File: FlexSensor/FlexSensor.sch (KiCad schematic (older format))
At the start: 167 parts

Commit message: Added ethernet
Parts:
- added C?: 470pF, symbol Device:C_Small
- added C?: 1µF, symbol Device:C_Small
- added C?: 4.7µF, symbol Device:C_Small
- added C? (x4): 100nF, symbol Device:C_Small
- added C?: 22nF, symbol Device:C_Small
- added J?: 8P8C_LED, symbol Connector:8P8C_LED
- added L?: FB 2.0A/0.050 DCR, symbol Device:Ferrite_Bead_Small
- added R? (x2): 330, symbol Device:R
- added R?: 100, symbol Device:R
- added R?: 12K, symbol Device:R
- added R? (x4): 49.9, symbol Device:R
- added R? (x2): 33, symbol Device:R
- added U?: LAN8720A, Package_DFN_QFN:QFN-24-1EP_4x4mm_P0.5mm_EP2.6x2.6mm, symbol Interface_Ethernet:LAN8720A
- added U?: JYSP75S4, symbol Trainiot:JYSP75S4
- R? (x2): value 10K -> 12K
- R?: value 10K -> 36K
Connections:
- net labels added: BOOTED, ETH_LED1, ETH_LED2
- net labels removed: RMII_EXT_OSC_CLK
- wire segments 864 -> 961
- no-connect marks 24 -> 28
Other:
- note added: "Check which led is 1 and which is 2 in the pinout"
- note added: "Ethernet"
- note added: "Just an inverter, can\nbe replaced"
- moved on the sheet: C?, D?, Q?, R?, U?, U?A

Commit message: Added pull up to shift register output for S88
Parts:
- added R? (x4): 36K, symbol Device:R
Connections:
- wire segments 961 -> 973
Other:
- moved on the sheet: C?, U?

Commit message: Working on adding LocoNet
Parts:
- removed U?: ULN2003A, symbol Transistor_Array:ULN2003A
- added C?: 4.7µF, symbol Device:C_Small
- added D?: 1N4148, Diode_THT:D_DO-35_SOD27_P7.62mm_Horizontal, symbol Diode:1N4148
- added D? (x2): LED, symbol Device:LED
- added J? (x2): 6P6C, symbol Connector:6P6C
- added Q?: BC817, Package_TO_SOT_SMD:SOT-23, symbol Transistor_BJT:BC817
- added R?: 27K, symbol Device:R
- added R?: 180K, symbol Device:R
- added R? (x2): 10K, symbol Device:R
- added R?: 240K, symbol Device:R
- added R?: 56K, symbol Device:R
- added R?: 22K, symbol Device:R
- added R?: 1K, symbol Device:R
- added R? (x2): 330, symbol Device:R
- added U?: ULN2803A, symbol Transistor_Array:ULN2803A
- added U? (x2): LM393, symbol Comparator:LM393
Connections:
- net labels added: PULL_DOWN_0, PULL_DOWN_1
- net labels removed: PULL_DOWN
- wire segments 973 -> 1056
- no-connect marks 28 -> 27
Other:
- note added: "Invert????????????????"
- note added: "Transmit LED? Maybe use fact tx and rx are identical in transmit?"
- note removed: "Cheap level shifter without pullup?"
- note removed: "ULN2803A could drive a second pull down,\nfor 3 different pull down values \nusing one extra GPIO pin."
- moved on the sheet: R?

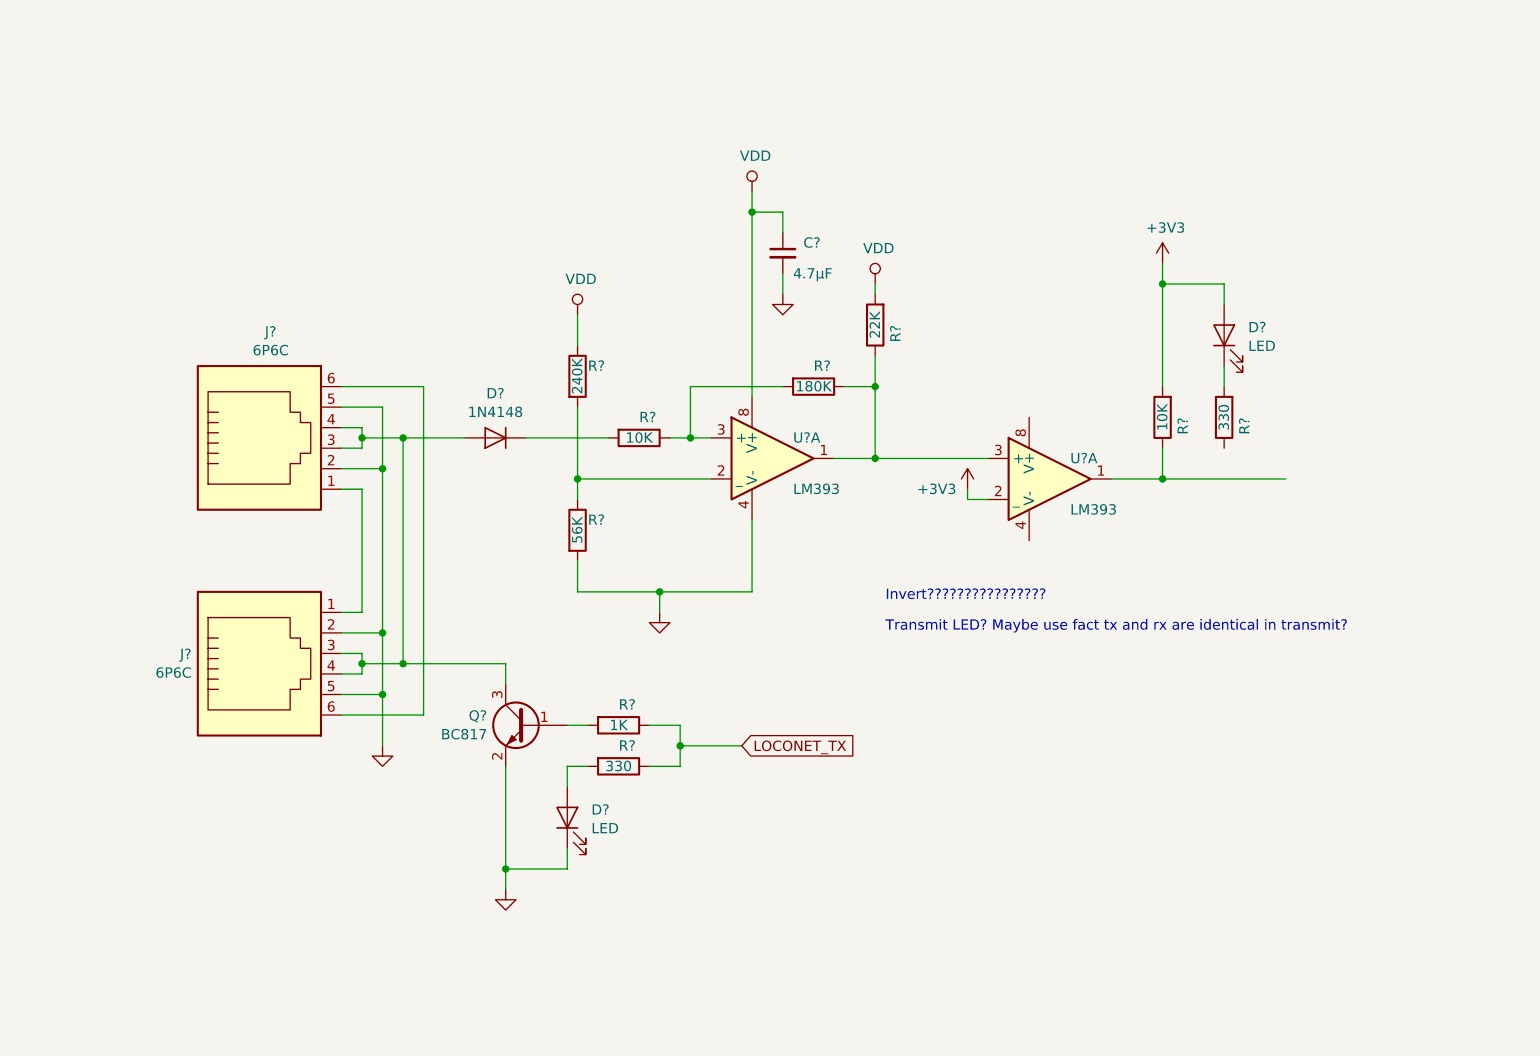
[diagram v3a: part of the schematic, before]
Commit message: Added LocoNet
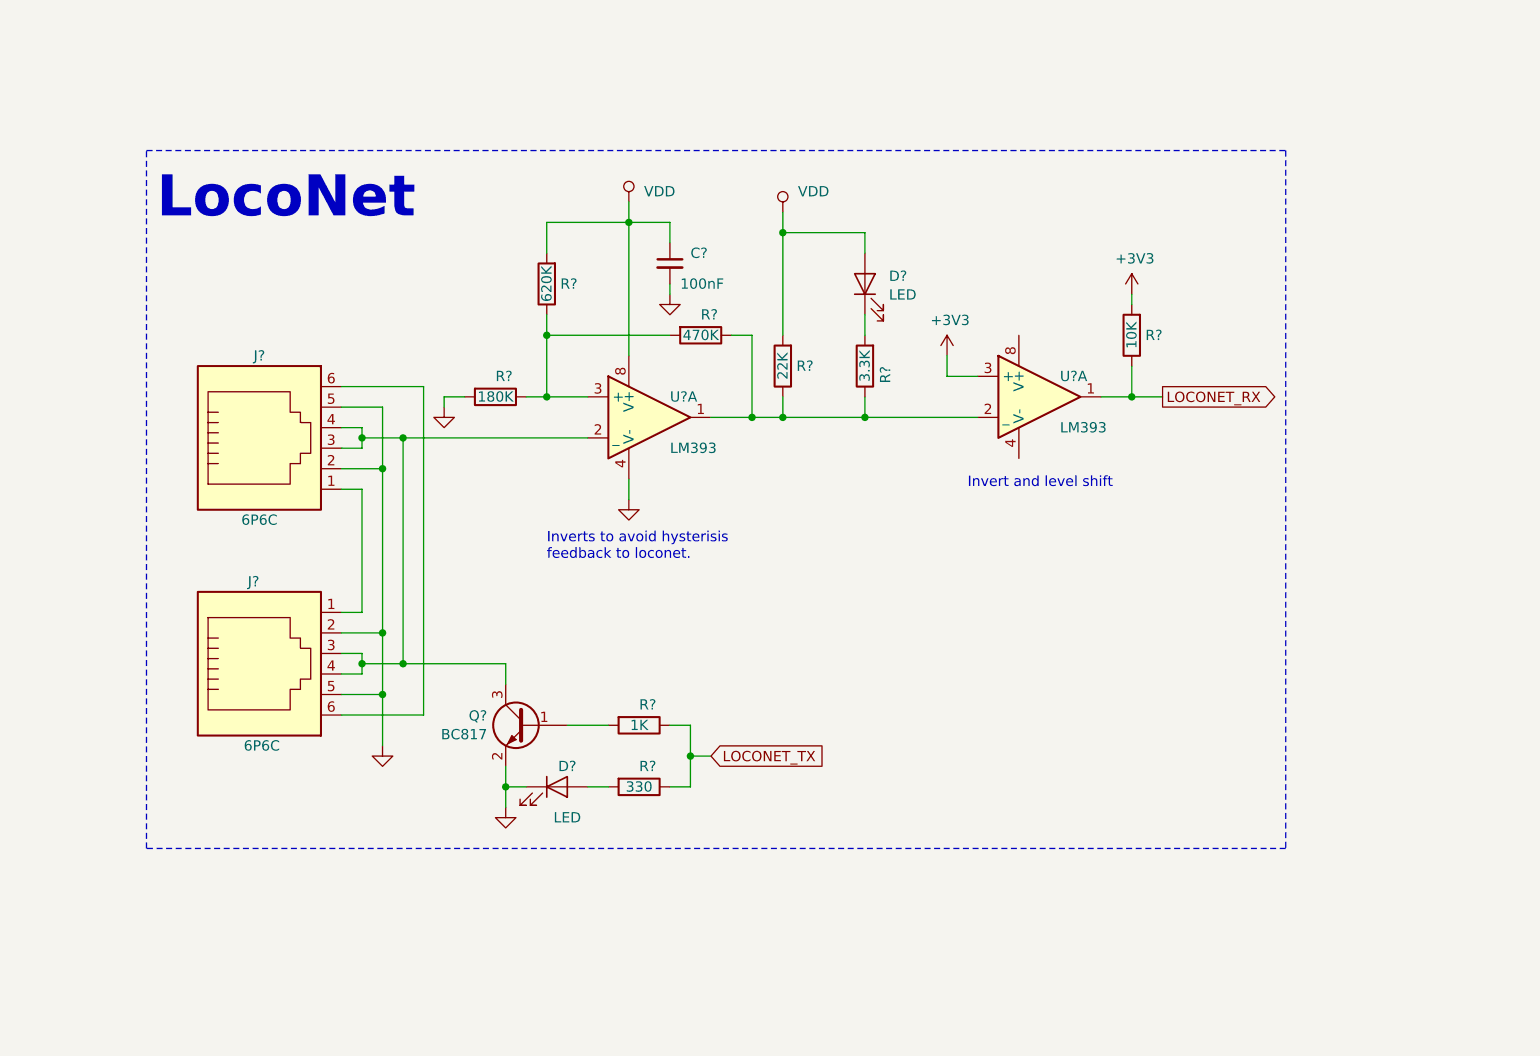
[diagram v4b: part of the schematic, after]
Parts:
- removed D?: 1N4148, Diode_THT:D_DO-35_SOD27_P7.62mm_Horizontal, symbol Diode:1N4148
- removed R?: 180K, symbol Device:R
- removed R? (x2): 10K, symbol Device:R
- removed R?: 240K, symbol Device:R
- removed R?: 56K, symbol Device:R
- removed R?: 22K, symbol Device:R
- removed U?: LM393, symbol Comparator:LM393
- added R?: 180K, symbol Device:R
- added R?: 620K, symbol Device:R
- added R?: 470K, symbol Device:R
- added R?: 22K, symbol Device:R
- added R?: 10K, symbol Device:R
- added U?: LM393, symbol Comparator:LM393
- C?: value 4.7µF -> 100nF
- R?: value 330 -> 3.3K
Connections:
- net +3V3: now also R?.2, R?.2, R?.2, U?.3 (+)
- net GND: now also R?.2
- net LOCONET_RX: now also R?.1, U?.1
- net at J?.3, J?.3, J?.4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: now also U?.2 (_)
- net at U?.1: now also R?.1, R?.1, R?.1, U?.2 (_)
- net at U?.3 (+): now also R?.1, R?.1, R?.2
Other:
- note added: "Invert and level shift"
- note added: "Inverts to avoid hysterisis\nfeedback to loconet."
- note added: "LocoNet"
- note removed: "Invert????????????????"
- note removed: "Transmit LED? Maybe use fact tx and rx are identical in transmit?"
- moved on the sheet: C?, D?, R?, U?A

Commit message: Added xpressnet and GPIO. Rearranged schematic to fit in A1.
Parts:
- added C?: 100nF, symbol Device:C_Small
- added D? (x2): LED, symbol Device:LED
- added J? (x2): 6P6C, symbol Connector:6P6C
- added J?: GPIO, symbol Connector:Conn_01x06_Male
- added R?: 120, symbol Device:R
- added R? (x2): 330, symbol Device:R
- added SW?: XPRESSNET_TERM, symbol Switch:SW_DIP_x01
- added U?: MAX3082, symbol Interface_UART:MAX3485
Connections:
- net UART_CTS is gone; now on net LOCONET_RX: U?.6 (IO34)
- net UART_RX is gone; now on net XPRESSNET_RX: U?.7 (IO35)
- net UART_TX is gone; now on net XPRESSNET_TX: U?.8 (IO32)
- net +3V3: now also C?.1, J?.1 (Pin_1), U?.8 (VCC)
- net GND: now also C?.2, J?.2, J?.2, J?.6 (Pin_6), U?.5 (GND)
- net LOCONET_RX: no longer U?.28 (IO17)
- net XPRESSNET_RX: now also R?.1, U?.1 (RO); no longer U?.13 (IO14)
- net XPRESSNET_TX: now also D?.1 (K), U?.4 (DI); no longer U?.14 (IO12)
- net XPRESSNET_TX_ENABLE: now also D?.1 (K), R?.1, U?.2 (~RE), U?.3 (DE)
- net UART_RTS renamed GPIO_1
- net GPIO_1: now also J?.2 (Pin_2)
- new net: J?.4, J?.4, SW?.1, U?.6 (A)
- new net: J?.3, J?.3, R?.1, U?.7 (B)
- new net: J?.1, J?.1
- new net: J?.5, J?.5
- new net: J?.6, J?.6
- new net: R?.2, SW?.2
- new net: D?.2 (A), R?.2 (x2)
- new net GPIO_2: J?.3 (Pin_3), U?.13 (IO14)
- new net GPIO_3: J?.4 (Pin_4), U?.14 (IO12)
- new net GPIO_4: J?.5 (Pin_5), U?.28 (IO17)
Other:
- note added: "Alternatives\nin order of\nrecommendation:\nMAX3085\nMAX3088\nMAX3485"
- note added: "Boot status"
- note added: "Button + Status LED"
- note added: "ESP32-WROOM"
- note added: "ExpressNet"
- note added: "GPIO"
- note added: "GPIO Expansion"
- note added: "XPRESSNET on single IO? Reuse tx/rx based on direction?\nFast enough? Noise on the line when changing?"
- note removed: "Single output, better scaling.\nConsider merging offset and scaling"
- moved on the sheet: C?, D?, J?, L?, Q?, R?, SW?, TP?, U?, U?A, U?B, U?C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

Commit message: Minor rearrangement of GPIO pins.
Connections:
- net GPIO_1: now also U?.27 (IO16); no longer U?.9 (IO33)
- net LOCONET_TX: now also U?.9 (IO33); no longer U?.27 (IO16)
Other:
- note removed: "If gates are available,\ncould add reset and\n"present" if +5V detected"
- moved on the sheet: Q?, R?
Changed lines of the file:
@@
 	0    1    1    0
 $EndComp
-Text GLabel 17700 1500 0    50   Input ~ 0
+Text GLabel 17550 2000 0    50   Input ~ 0
 ~DTR
-Text GLabel 17700 2250 0    50   Input ~ 0
+Text GLabel 17550 2750 0    50   Input ~ 0
 ~RTS
 $Comp
 L Transistor_BJT:BC817 Q?
 U 1 1 5B3FBC09
-P 18700 1500
-F 0 "Q?" H 18891 1546 50  0000 L CNN
-F 1 "BC817" H 18891 1455 50  0000 L CNN
-F 2 "Package_TO_SOT_SMD:SOT-23" H 18900 1425 50  0001 L CIN
-F 3 "http://www.fairchildsemi.com/ds/BC/BC817.pdf" H 18700 1500 50  0001 L CNN
-	1    18700 1500
+P 18550 2000
+F 0 "Q?" H 18741 2046 50  0000 L CNN
+F 1 "BC817" H 18741 1955 50  0000 L CNN
+F 2 "Package_TO_SOT_SMD:SOT-23" H 18750 1925 50  0001 L CIN
+F 3 "http://www.fairchildsemi.com/ds/BC/BC817.pdf" H 18550 2000 50  0001 L CNN
+	1    18550 2000
 	1    0    0    -1
 $EndComp
@@
 L Transistor_BJT:BC817 Q?
 U 1 1 5B3FBD2F
-P 18700 2250
-F 0 "Q?" H 18891 2204 50  0000 L CNN
-F 1 "BC817" H 18891 2295 50  0000 L CNN
-F 2 "Package_TO_SOT_SMD:SOT-23" H 18900 2175 50  0001 L CIN
-F 3 "http://www.fairchildsemi.com/ds/BC/BC817.pdf" H 18700 2250 50  0001 L CNN
-	1    18700 2250
+P 18550 2750
+F 0 "Q?" H 18741 2704 50  0000 L CNN
+F 1 "BC817" H 18741 2795 50  0000 L CNN
+F 2 "Package_TO_SOT_SMD:SOT-23" H 18750 2675 50  0001 L CIN
+F 3 "http://www.fairchildsemi.com/ds/BC/BC817.pdf" H 18550 2750 50  0001 L CNN
+	1    18550 2750
 	1    0    0    1
 $EndComp
@@
 L Device:R R?
 U 1 1 5B45C0C3
-P 18150 2250
-F 0 "R?" V 18050 2200 50  0000 L CNN
-F 1 "12K" V 18150 2250 50  0000 C CNN
-F 2 "" V 18080 2250 50  0001 C CNN
-F 3 "~" H 18150 2250 50  0001 C CNN
-	1    18150 2250
+P 18000 2750
+F 0 "R?" V 17900 2700 50  0000 L CNN
+F 1 "12K" V 18000 2750 50  0000 C CNN
+F 2 "" V 17930 2750 50  0001 C CNN
+F 3 "~" H 18000 2750 50  0001 C CNN
+	1    18000 2750
 	0    1    1    0
 $EndComp
 Wire Wire Line
-	18300 2250 18500 2250
+	18150 2750 18350 2750
 Wire Wire Line
-	18000 2250 17900 2250
+	17850 2750 17750 2750
 $Comp
 L Device:R R?
 U 1 1 5B57DA9E
-P 18150 1500
-F 0 "R?" V 18050 1450 50  0000 L CNN
-F 1 "12K" V 18150 1500 50  0000 C CNN
-F 2 "" V 18080 1500 50  0001 C CNN
-F 3 "~" H 18150 1500 50  0001 C CNN
-	1    18150 1500
+P 18000 2000
+F 0 "R?" V 17900 1950 50  0000 L CNN
+F 1 "12K" V 18000 2000 50  0000 C CNN
+F 2 "" V 17930 2000 50  0001 C CNN
+F 3 "~" H 18000 2000 50  0001 C CNN
+	1    18000 2000
 	0    1    1    0
 $EndComp
 Wire Wire Line
-	18300 1500 18500 1500
+	18150 2000 18350 2000
 Wire Wire Line
-	18000 1500 17800 1500
+	17850 2000 17650 2000
 Wire Wire Line
-	17800 1500 17800 1950
+	17650 2000 17650 2450
 Wire Wire Line
-	17800 1950 18800 1950
+	17650 2450 18650 2450
 Wire Wire Line
-	18800 1950 18800 2050
-Connection ~ 17800 1500
+	18650 2450 18650 2550
+Connection ~ 17650 2000
 Wire Wire Line
-	17800 1500 17700 1500
+	17650 2000 17550 2000
 Wire Wire Line
-	18800 2450 18800 2550
+	18650 2950 18650 3050
 Wire Wire Line
-	18800 1700 18800 1800
+	18650 2200 18650 2300
 Wire Wire Line
-	18800 1800 17900 1800
+	18650 2300 17750 2300
 Wire Wire Line
-	17900 1800 17900 2250
-Connection ~ 17900 2250
+	17750 2300 17750 2750
+Connection ~ 17750 2750
 Wire Wire Line
-	17900 2250 17700 2250
+	17750 2750 17550 2750
 Wire Wire Line
-	18800 1300 18800 1200
+	18650 1800 18650 1700
 Wire Wire Line
-	18800 1200 19200 1200
-Text GLabel 19200 1200 2    50   Output ~ 0
+	18650 1700 19050 1700
+Text GLabel 19050 1700 2    50   Output ~ 0
 EN
 Text GLabel 16300 5500 0    50   Input ~ 0
@@
 Text GLabel 16300 5800 0    50   Input ~ 0
 LOCONET_RX
-Text GLabel 18350 6400 2    50   Output ~ 0
+Text GLabel 16300 6100 0    50   Output ~ 0
 LOCONET_TX
 Wire Wire Line
@@
 Wire Wire Line
 	11800 11500 11100 11500
-Text GLabel 16300 6100 0    50   BiDi ~ 0
+Text GLabel 18350 6400 2    50   BiDi ~ 0
 GPIO_1
 Text GLabel 8500 9000 0    50   Input ~ 0
@@
 Wire Wire Line
 	3200 21900 2850 21900
-Text Notes 3050 18700 0    50   ~ 0
-If gates are available,\ncould add reset and\n"present" if +5V detected
 Text GLabel 7100 21900 0    50   Input ~ 0
 ~S88_OUT_RESET
@@
 	15700 18750 15700 18850
 Wire Wire Line
-	18800 2550 19200 2550
+	18650 3050 19050 3050
 Wire Wire Line
 	10700 5300 10550 5300
@@
 Wire Wire Line
 	9350 5450 9100 5450
-Text GLabel 19200 2550 2    50   Output ~ 0
+Text GLabel 19050 3050 2    50   Output ~ 0
 IO0
 Text GLabel 11700 19200 0    50   Output ~ 0

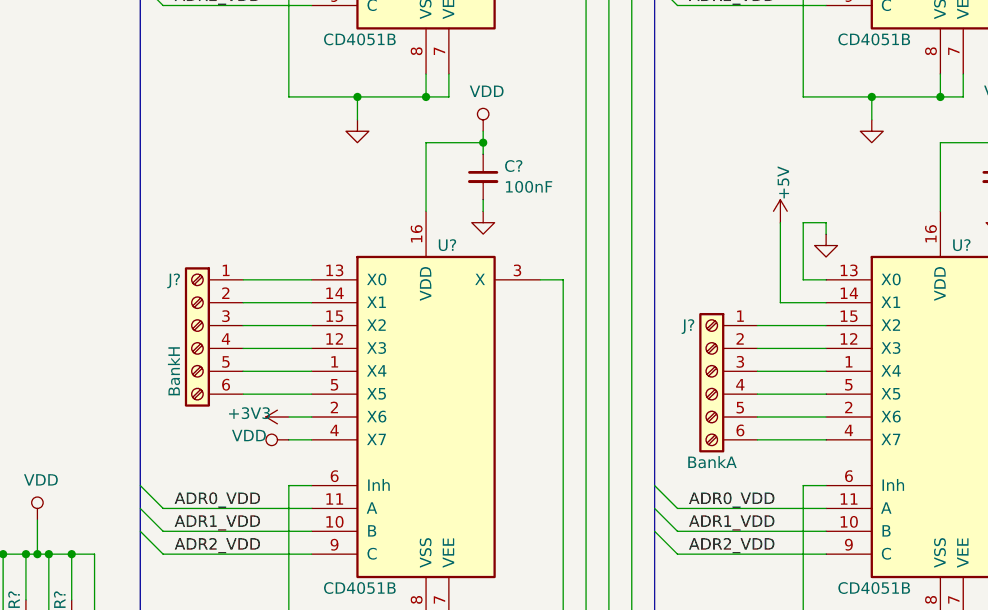
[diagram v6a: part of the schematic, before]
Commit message: Changed reference voltages in the inputs to avoid having 5V mandatory. Added a pull up instead. Not sure how usefull it will be, but I do not really need the extra input.
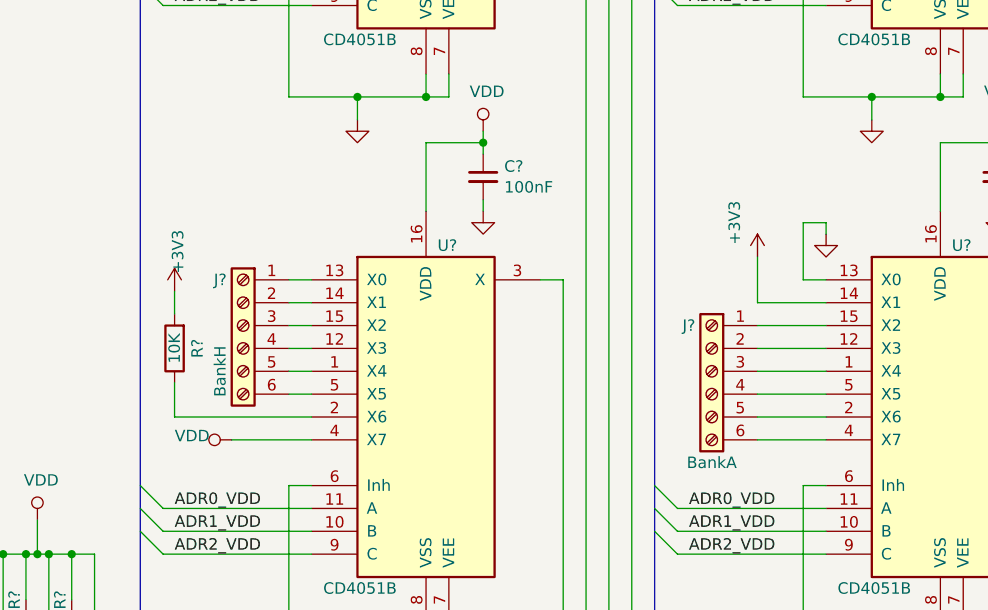
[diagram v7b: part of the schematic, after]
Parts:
- added R?: 10K, symbol Device:R
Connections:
- net +3V3: now also U?.14 (X1), R?.2; no longer U?.2 (X6)
- net +5V: no longer U?.14 (X1)
- new net: R?.1, U?.2 (X6)
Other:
- moved on the sheet: J?
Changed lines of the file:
@@
 $EndComp
 Wire Wire Line
-	3350 13250 3450 13250
+	3100 13250 3450 13250
 Wire Wire Line
-	3450 13150 3350 13150
+	3350 13050 3450 13050
 Wire Wire Line
-	3150 13050 3450 13050
+	3450 12950 3350 12950
 Wire Wire Line
-	3450 12950 3150 12950
+	3350 12850 3450 12850
 Wire Wire Line
-	3150 12850 3450 12850
+	3450 12750 3350 12750
 Wire Wire Line
-	3450 12750 3150 12750
+	3350 12650 3450 12650
 Wire Wire Line
-	3150 12650 3450 12650
-Wire Wire Line
-	3450 12550 3150 12550
+	3450 12550 3350 12550
 Wire Wire Line
 	3450 13450 3350 13450
@@
 	5700 12750 5400 12750
 Wire Wire Line
-	5500 12650 5700 12650
+	5400 12650 5700 12650
 Wire Wire Line
 	5700 12550 5600 12550
@@
 	5700 12300 5700 12350
 Wire Wire Line
-	5500 12300 5500 12650
+	2850 13000 2850 13150
 $Comp
 L power:VDD #PWR?
 U 1 1 5F1B28F5
-P 3350 13250
-F 0 "#PWR?" H 3350 13100 50  0001 C CNN
-F 1 "VDD" V 3367 13423 50  0000 C CNN
-F 2 "" H 3350 13250 50  0001 C CNN
-F 3 "" H 3350 13250 50  0001 C CNN
-	1    3350 13250
+P 3100 13250
+F 0 "#PWR?" H 3100 13100 50  0001 C CNN
+F 1 "VDD" V 3117 13423 50  0000 C CNN
+F 2 "" H 3100 13250 50  0001 C CNN
+F 3 "" H 3100 13250 50  0001 C CNN
+	1    3100 13250
 	0    -1   -1   0
 $EndComp
 $Comp
-L power:+5V #PWR?
-U 1 1 5F2373F6
-P 5500 12300
-F 0 "#PWR?" H 5500 12150 50  0001 C CNN
-F 1 "+5V" V 5515 12473 50  0000 C CNN
-F 2 "" H 5500 12300 50  0001 C CNN
-F 3 "" H 5500 12300 50  0001 C CNN
-	1    5500 12300
-	1    0    0    -1
-$EndComp
-$Comp
 L power:+3V3 #PWR?
 U 1 1 5F237555
-P 3350 13150
-F 0 "#PWR?" H 3350 13000 50  0001 C CNN
-F 1 "+3V3" V 3365 13323 50  0000 C CNN
-F 2 "" H 3350 13150 50  0001 C CNN
-F 3 "" H 3350 13150 50  0001 C CNN
-	1    3350 13150
-	0    -1   -1   0
+P 5400 12450
+F 0 "#PWR?" H 5400 12300 50  0001 C CNN
+F 1 "+3V3" V 5300 12600 50  0000 C CNN
+F 2 "" H 5400 12450 50  0001 C CNN
+F 3 "" H 5400 12450 50  0001 C CNN
+	1    5400 12450
+	1    0    0    -1
 $EndComp
 $Comp
@@
 L Connector:Screw_Terminal_01x06 J?
 U 1 1 5F2BE783
-P 2950 12750
-F 0 "J?" H 3050 12950 50  0000 C CNN
-F 1 "BankH" V 3050 12550 50  0000 C CNN
-F 2 "" H 2950 12750 50  0001 C CNN
-F 3 "~" H 2950 12750 50  0001 C CNN
-	1    2950 12750
+P 3150 12750
+F 0 "J?" H 3250 12950 50  0000 C CNN
+F 1 "BankH" V 3250 12550 50  0000 C CNN
+F 2 "" H 3150 12750 50  0001 C CNN
+F 3 "~" H 3150 12750 50  0001 C CNN
+	1    3150 12750
 	-1   0    0    -1
 $EndComp
@@
 Text Notes 12350 4700 0    200  ~ 40
 GPIO
+$Comp
+L Device:R R?
+U 1 1 62D1248E
+P 2850 12850
+F 0 "R?" V 2750 12850 50  0000 C CNN
+F 1 "10K" V 2850 12850 50  0000 C CNN
+F 2 "" V 2780 12850 50  0001 C CNN
+F 3 "~" H 2850 12850 50  0001 C CNN
+	1    2850 12850
+	-1   0    0    1
+$EndComp
+Wire Wire Line
+	2850 12700 2850 12600
+$Comp
+L power:+3V3 #PWR?
+U 1 1 62F682EA
+P 2850 12600
+F 0 "#PWR?" H 2850 12450 50  0001 C CNN
+F 1 "+3V3" V 2865 12773 50  0000 C CNN
+F 2 "" H 2850 12600 50  0001 C CNN
+F 3 "" H 2850 12600 50  0001 C CNN
+	1    2850 12600
+	1    0    0    -1
+$EndComp
+Wire Wire Line
+	2850 13150 3450 13150
+Wire Wire Line
+	5400 12450 5400 12650
 Wire Bus Line
 	3350 14400 4950 14400
